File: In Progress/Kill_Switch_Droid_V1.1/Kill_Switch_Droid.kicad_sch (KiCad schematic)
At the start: 49 parts, among them J1 USB_B_Micro, J2 Power In, J3 U.FL-R-SMT-1(10), J4 External Switch In, J5 Output, Q2 UMH3N, Q3 BSS138, U1 ESP32-PICO-MINI-02, U2 CP2102N-A02-GQFN28, U3 LP5912-3.3DRV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

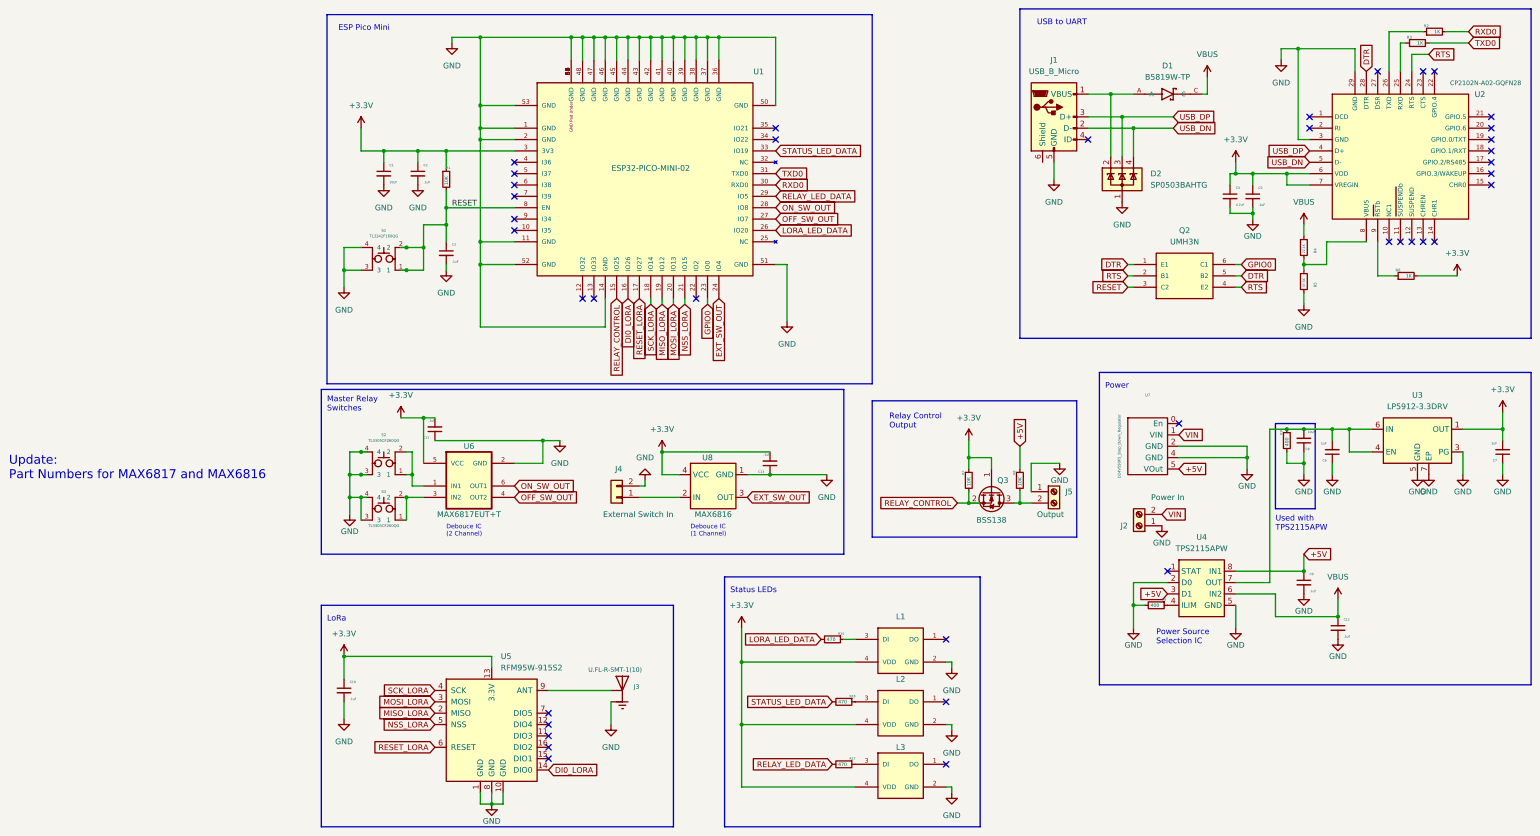
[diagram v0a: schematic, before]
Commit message: Updating the Kill Switch Droid side
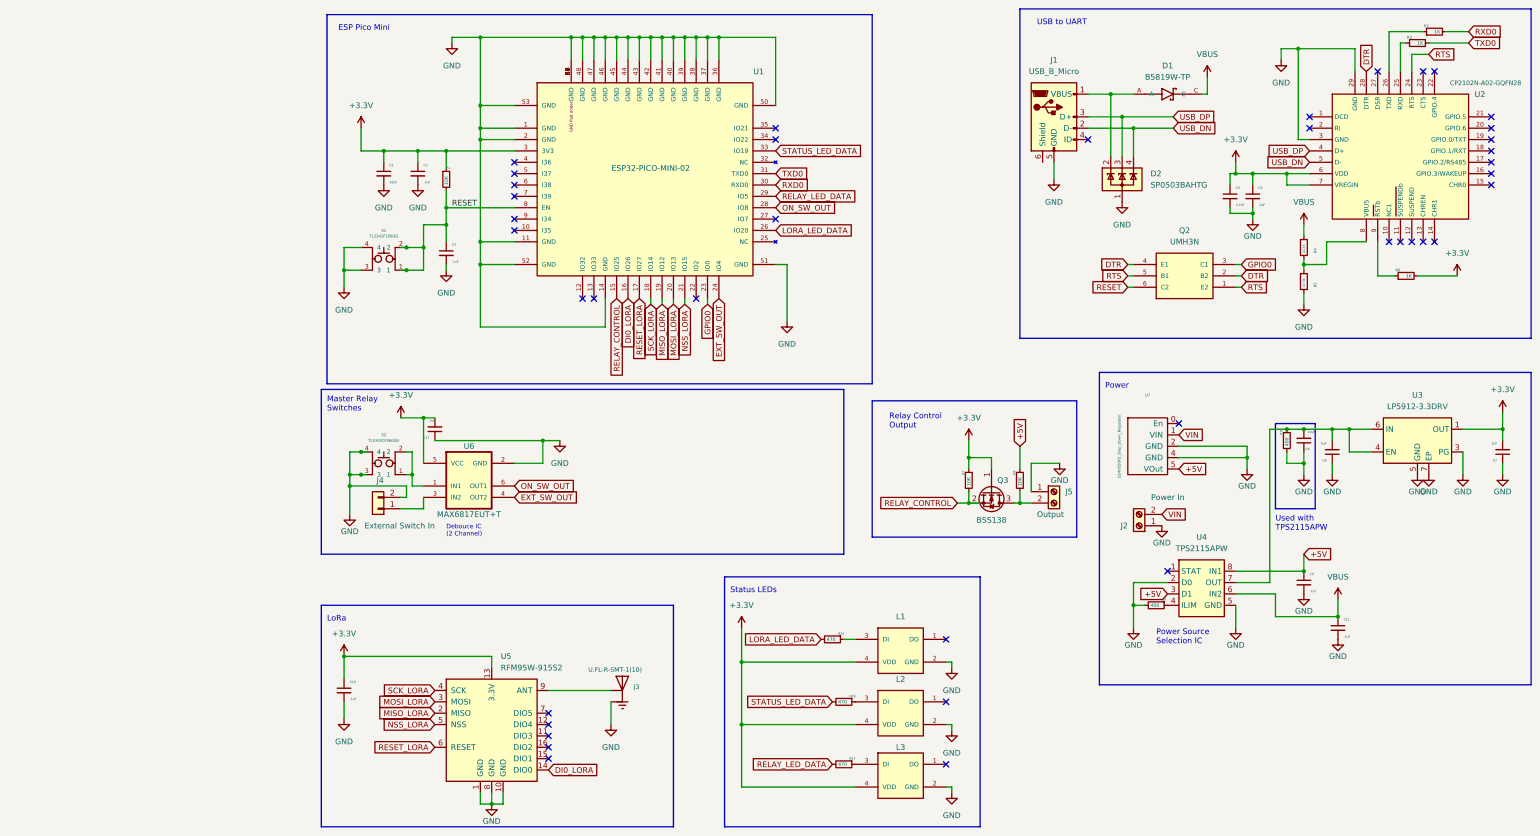
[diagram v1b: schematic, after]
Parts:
- removed C13: .1uF, Capacitor_SMD:C_0603_1608Metric, symbol Device:C_Small
- removed S3: TL3305CF260QG, Custom:TL3305CF260QG, symbol Custom:TL3342F160QG
- removed U8: MAX6816, Package_TO_SOT_SMD:SOT-143, symbol Interface:MAX6816
- Q2: footprint Custom:SOT65P230X110-6N -> SOT65P230X110-6N
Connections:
- net DTR: now also Q2.2 (B2), Q2.4 (E1); no longer Q2.1 (E1), Q2.5 (B2)
- net EXT_SW_OUT: now also U6.4 (OUT2)
- net GPIO0: now also Q2.3 (C1); no longer Q2.6 (C1)
- net RESET: now also Q2.6 (C2); no longer Q2.3 (C2)
- net RTS: now also Q2.1 (E2), Q2.5 (B1); no longer Q2.2 (B1), Q2.4 (E2)
- net at U6.3 (IN2): now also J4.1 (Pin_1)
- net OFF_SW_OUT: no longer names the net of U1.27 (IO7)
- net OFF_SW_OUT: no longer U6.4 (OUT2)
- no-connect marks 39 -> 40
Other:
- note removed: "Debouce IC (1 Channel)"
- note removed: "Update: Part Numbers for MAX6817 and MAX6816"
- moved on the sheet: J4

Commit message: some minor updates
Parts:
- removed J3: U.FL-R-SMT-1(10), Custom:HRS_U.FL-R-SMT-1(10), symbol Custom:U.FL-R-SMT-1(10)
- added J3: 73391-0083, Custom:73391-0083, symbol Custom:73391-0083
- added J6: Conn_01x03, Connector_Molex:Molex_KK-254_AE-6410-03A_1x03_P2.54mm_Vertical, symbol Connector_Generic:Conn_01x03
- C1: Digikey Part Number 732-7624-1-ND -> (none); LCSC ----- -> C1222438; Manufacturer's Part Number (none) -> CS2012X7R106K100NRE; Manufacturers Part Number 885012107014 -> CS2012X7R106K100NRE; Mouser Part Number 710-885012107014 -> (none)
- C10, C11, C12, C2, C3, C5, C9: footprint Capacitor_SMD:C_0603_1608Metric -> Capacitor_SMD:C_0402_1005Metric; Digikey Part Number 732-7939-1-ND -> (none); LCSC ----- -> C307331; Manufacturers Name Würth Elektronik -> Samsung Electro-Mechanics; Manufacturers Part Number 885012206020 -> CL05B104KB54PNC; Mouser Part Number 710-885012206020 -> (none)
- C4: footprint Capacitor_SMD:C_0603_1608Metric -> Capacitor_SMD:C_0805_2012Metric; Digikey Part Number 732-7902-1-ND -> (none); LCSC ----- -> C126590; Manufacturers Name Würth Elektronik -> Murata Electronics; Manufacturers Part Number 885012106005 -> GCM21BR71C475KA67L; Mouser Part Number 710-885012106005 -> (none)
- C6, C7: Digikey Part Number 732-7971-1-ND -> (none); LCSC C2170528 -> C913562; Manufacturers Name Würth Elektronik -> Murata Electronics; Manufacturers Part Number 885012206052 -> GRM188B31H105KAALD; Mouser Part Number 710-885012206052 -> (none)
- C8: Digikey Part Number 732-7624-1-ND -> (none); LCSC ----- -> C1222438; Manufacturers Name Würth Elektronik -> Samwha Capacitor; Manufacturers Part Number 885012107014 -> CS2012X7R106K100NRE; Mouser Part Number 710-885012107014 -> (none)
- J2, J5: Digikey Part Number 1920-1323-ND -> (none); LCSC ----- -> C8465; Manufacturers Name Altech Corporation -> Ningbo Kangnex Elec; Manufacturers Part Number 34.102 -> WJ500V-5.08-2P; Mouser Part Number 845-34.102 -> (none)
- J4: LCSC (none) -> C234180; Manufacturer (none) -> MOLEX; Manufacturer's Part Number (none) -> 22232021
- L1, L2, L3: Digikey Part Number 1528-4684-ND -> (none); Manufacturers Name Worldsemi/Adafruit -> Worldsemi; Manufacturers Part Number WS2812B-2020/4684 -> WS2812B-2020; Mouser Part Number 485-4684 -> (none)
- Q2: footprint SOT65P230X110-6N -> Custom:SOT65P230X110-6N
- Q3: Digikey Part Number BSS138DW-FDICT-ND -> (none); Mouser Part Number 621-BSS138DW-F -> (none)
- R10, R9: Digikey Part Number 13-RC0402JR-13220RLCT-ND -> (none); LCSC C3931306 -> C4044825; Manufacturers Name YAGEO -> Meritek; Manufacturers Part Number RC0402JR-13220RL -> CR204000F; Mouser Part Number 603-RC0402JR-13220RL -> (none)
- R14, R16, R17: Digikey Part Number 13-RC0402JR-13220RLCT-ND -> (none); LCSC C3931306 -> C852799; Manufacturers Part Number RC0402JR-13220RL -> RT0402BRD07470RL; Mouser Part Number 603-RC0402JR-13220RL -> (none)
- R7, R8: Digikey Part Number 13-RC0402JR-13220RLCT-ND -> (none); LCSC C3931306 -> C705657; Manufacturers Part Number RC0402JR-13220RL -> RT0402CRD0710KL; Mouser Part Number 603-RC0402JR-13220RL -> (none)
- S1: Digikey Part Number EG2531CT-ND -> (none); LCSC ------ -> C2886898; Manufacturers Part Number TL3342F160QG/TR -> TL3342F160QG; Mouser Part Number ------ -> (none)
- S2: Digikey Part Number EG5355CT-ND -> (none); Mouser Part Number 612-TL3305CF260QG -> (none)
- U3: Digikey Part Number 296-48933-1-ND -> (none); Mouser Part Number 595-LP5912Q3.3DRVTQ1 -> (none)
- U4: Manufacturers Part Number TPS2115APW -> TPS2115APWR
- U6: Digikey Part Number MAX6817EUT+TCT-ND -> (none); Mouser Part Number 700-MAX6817EUTT -> (none)
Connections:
- net GND: now also J3.1, J3.2, J3.3, J3.4, J6.1 (Pin_1)
- net at U5.9 (ANT): now also J3.5
- net TX_HEADER: now reaches U1.22 (IO2)
- net TX_HEADER: now also J6.2 (Pin_2)
- net RX_HEADER: now reaches U1.27 (IO7)
- net RX_HEADER: now also J6.3 (Pin_3)
- no-connect marks 40 -> 38
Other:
- note added: "0 left"
- note added: "5 left"
- note added: "G"
- note added: "NOT AVAILABLE"
